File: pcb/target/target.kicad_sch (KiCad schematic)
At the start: 4 parts, among them J1 Pogo_01x06_female, J2 Pogo_01x06_male, U1 ATtiny3216-S

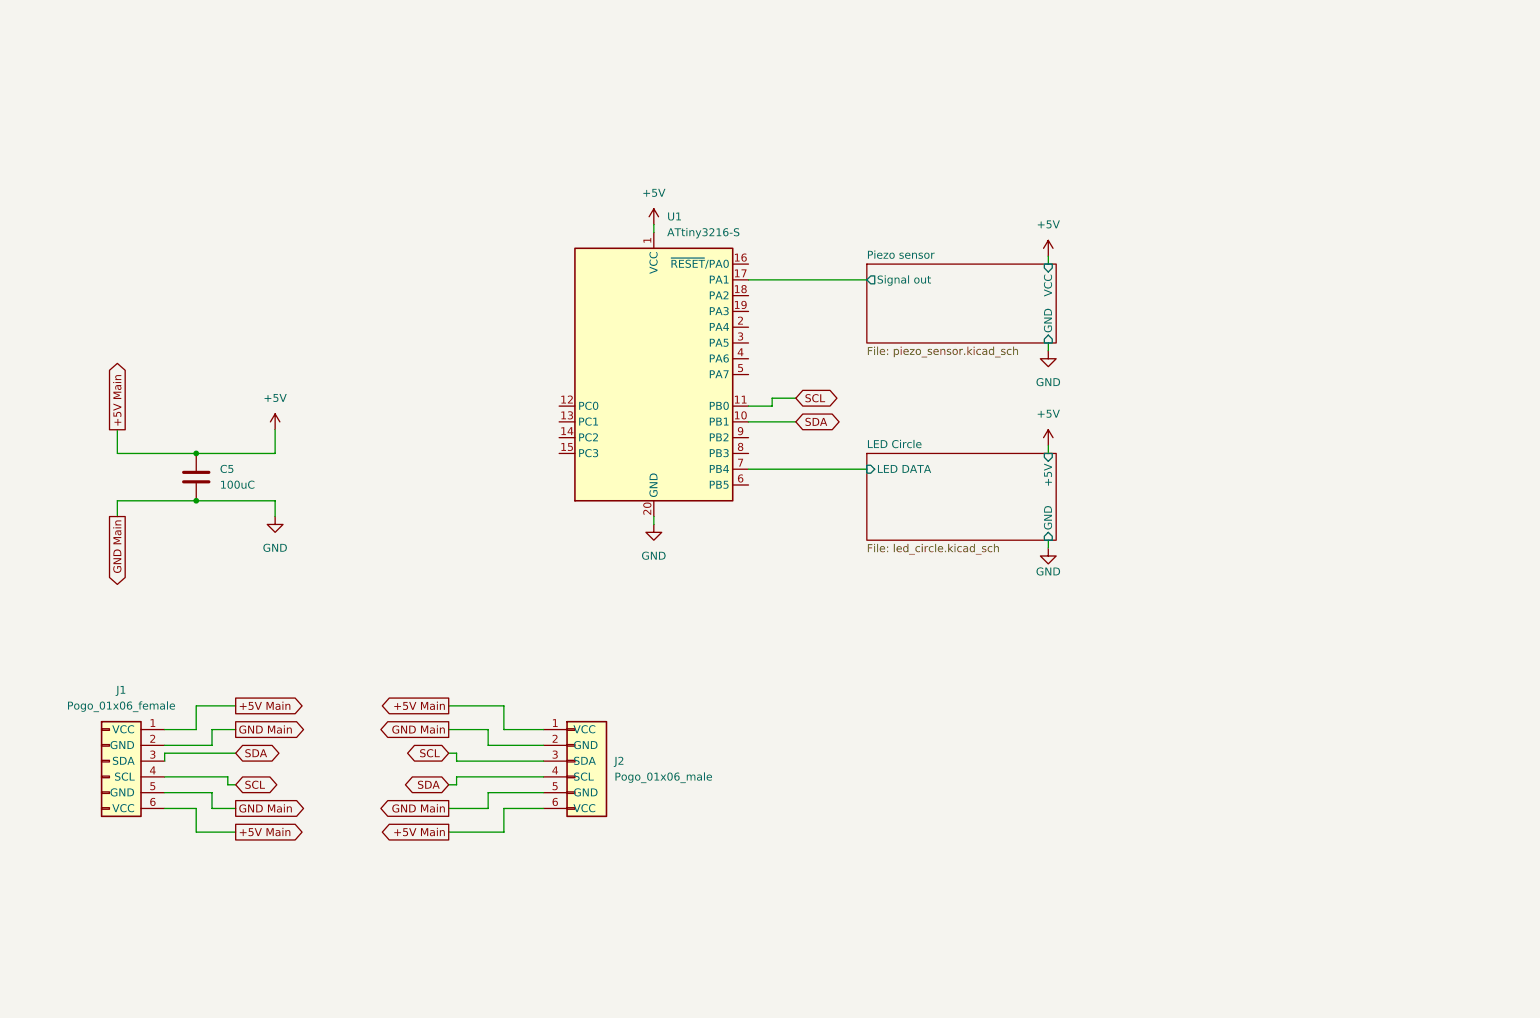
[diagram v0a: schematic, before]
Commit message: added updi connector
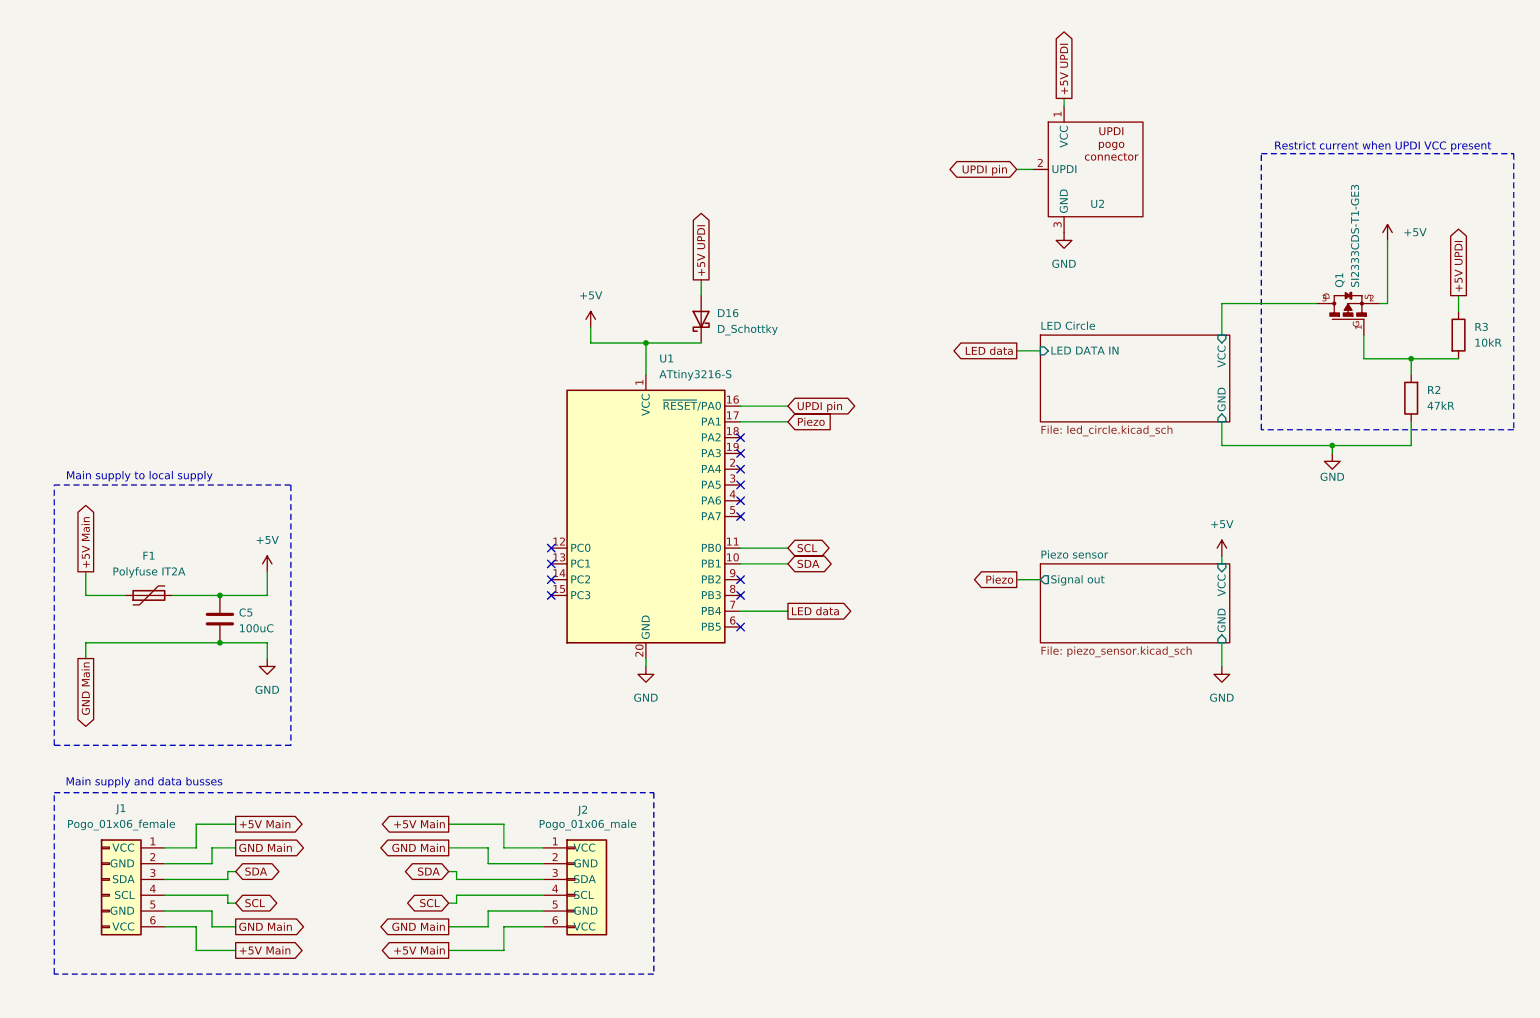
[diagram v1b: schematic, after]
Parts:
- added D16: D_Schottky, custom_footprints:BAT54_SOT23, symbol Device:D_Schottky
- added F1: Polyfuse IT2A, symbol Device:Polyfuse
- added Q1: SI2333CDS-T1-GE3, custom_footprints:SOT23, symbol SI2333CD:SI2333CDS-T1-GE3
- added R2: 47kR, symbol Device:R
- added R3: 10kR, symbol Device:R
- added U2: ~, updi_pogo:P2,54_MH3_pogo_updi, symbol updi_pogo:updi_pogo_connector
- J1, J2: footprint (none) -> Connector_Wire:SolderWire-1sqmm_1x06_P5.4mm_D1.4mm_OD2.7mm
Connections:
- net +5V: now also D16.1 (K), F1.2, Q1.2; no longer J1.1 (VCC), J1.6 (VCC), J2.1 (VCC), J2.6 (VCC)
- net GND: now also R2.1, U2.3 (GND)
- net SCL: now also J2.4 (SCL); no longer J2.3 (SDA)
- net SDA: now also J2.3 (SDA); no longer J2.4 (SCL)
- net UPDI pin: now reaches U1.16 (~{RESET}/PA0)
- net UPDI pin: now also U2.2 (UPDI)
- net LED Circle/LED DATA renamed LED data
- net Piezo sensor/Signal out renamed Piezo
- new net: Q1.1, R2.2, R3.2
- new net +5V Main: F1.1, J1.1 (VCC), J1.6 (VCC), J2.1 (VCC), J2.6 (VCC)
- new net +5V UPDI: D16.2 (A), R3.1, U2.1 (VCC)
- new net LED Circle/VCC: Q1.3
- no-connect marks 0 -> 13
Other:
- sheet LED Circle ports: added LED DATA IN, VCC; removed +5V, LED DATA
- note added: "Main supply and data busses"
- note added: "Main supply to local supply"
- note added: "Restrict current when UPDI VCC present"
- moved on the sheet: C5, J1, J2, U1

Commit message: fixed some footprint issues
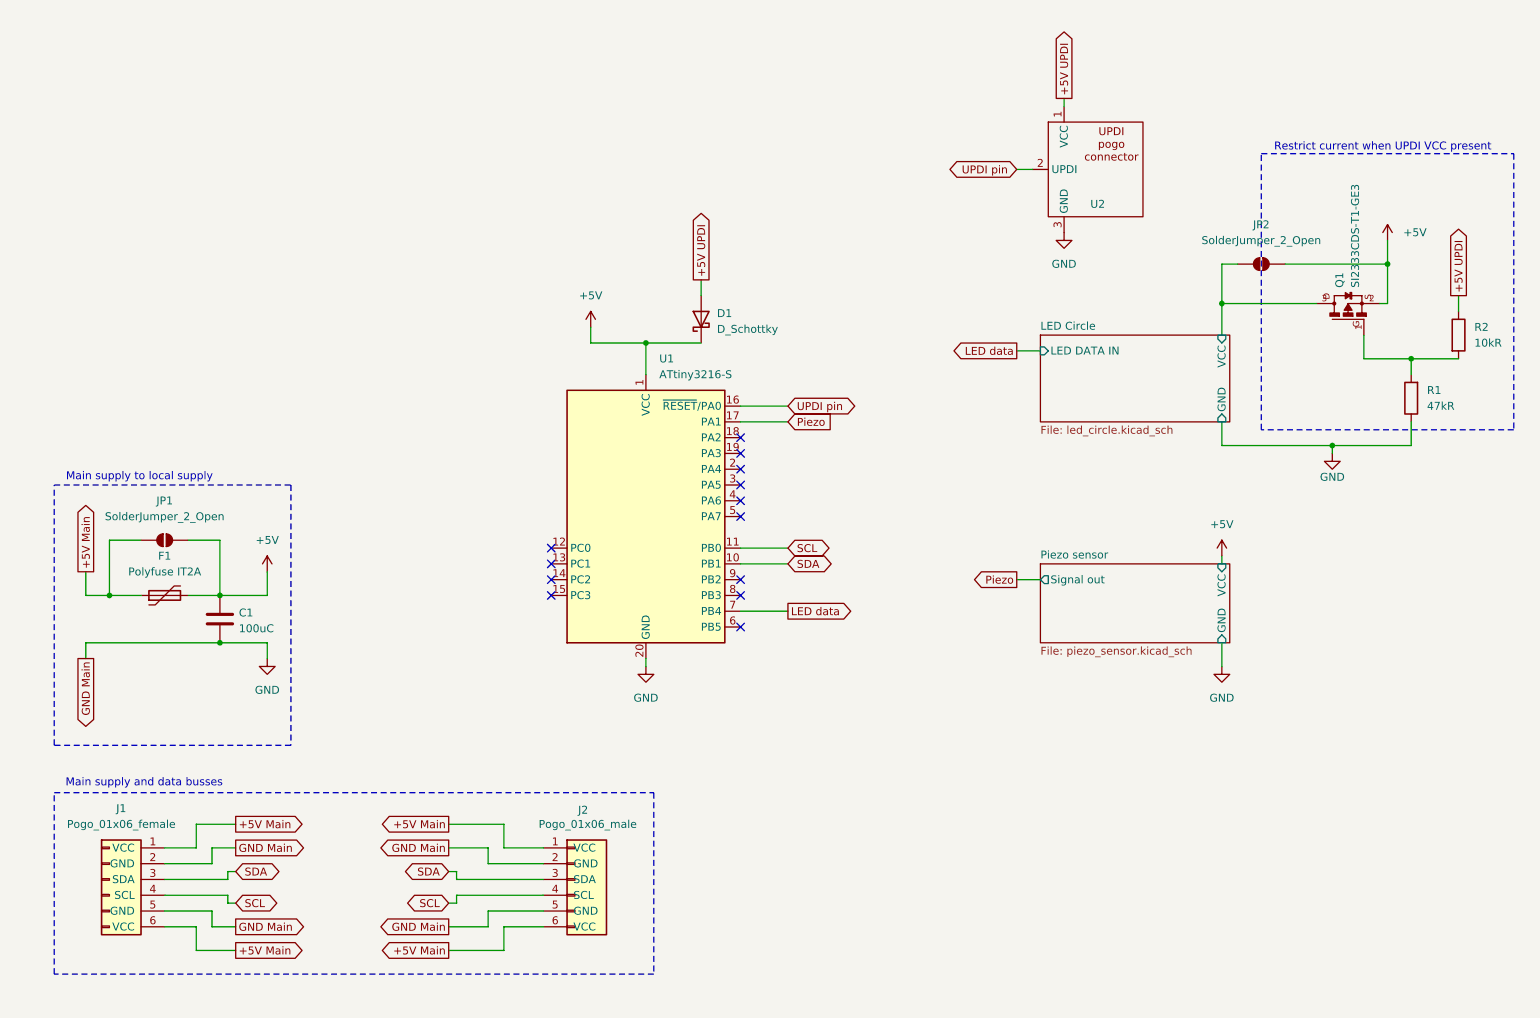
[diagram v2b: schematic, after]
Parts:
- added JP1, JP2: SolderJumper_2_Open, Jumper:SolderJumper-2_P1.3mm_Open_TrianglePad1.0x1.5mm, symbol Jumper:SolderJumper_2_Open
- F1: footprint (none) -> Fuse:Fuse_2920_7451Metric
- R1: renamed from R2; footprint (none) -> Resistor_SMD:R_1206_3216Metric
- R2: renamed from R3; footprint (none) -> Resistor_SMD:R_1206_3216Metric
- renumbered C5 to C1, D16 to D1
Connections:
- net +5V: now also JP1.2 (B), JP2.2 (B)
- net +5V Main: now also JP1.1 (A)
- net LED Circle/VCC: now also JP2.1 (A)
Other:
- moved on the sheet: F1

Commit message: finishing up target pcb
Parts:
- J1, J2: footprint Connector_Wire:SolderWire-1sqmm_1x06_P5.4mm_D1.4mm_OD2.7mm -> custom_footprints:01x06 SMD 4x4mm pad
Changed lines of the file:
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@@
 			)
 		)
-		(property "Footprint" "Connector_Wire:SolderWire-1sqmm_1x06_P5.4mm_D1.4mm_OD2.7mm"
+		(property "Footprint" "custom_footprints:01x06 SMD 4x4mm pad"
 			(at 101.6 175.26 0)
 			(effects
@@
 			)
 		)
-		(property "Footprint" "Connector_Wire:SolderWire-1sqmm_1x06_P5.4mm_D1.4mm_OD2.7mm"
+		(property "Footprint" "custom_footprints:01x06 SMD 4x4mm pad"
 			(at 26.67 175.26 0)
 			(effects

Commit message: retraced target pcb
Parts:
- removed JP1: SolderJumper_2_Open, Jumper:SolderJumper-2_P1.3mm_Open_TrianglePad1.0x1.5mm, symbol Jumper:SolderJumper_2_Open
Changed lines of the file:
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@@
-	)
-	(junction
-		(at 26.67 129.54)
-		(diameter 0)
-		(color 0 0 0 0)
 	)
 	(junction
@@
 	(wire
 		(pts
-			(xy 44.45 120.65) (xy 44.45 129.54)
-		)
-		(stroke
-			(width 0)
-			(type default)
-		)
-	)
-	(wire
-		(pts
 			(xy 220.98 82.55) (xy 205.74 82.55)
 		)
@@
 	(wire
 		(pts
-			(xy 39.37 120.65) (xy 44.45 120.65)
-		)
-		(stroke
-			(width 0)
-			(type default)
-		)
-	)
-	(wire
-		(pts
 			(xy 128.27 121.92) (xy 135.89 121.92)
 		)
@@
 	(wire
 		(pts
-			(xy 26.67 120.65) (xy 26.67 129.54)
-		)
-		(stroke
-			(width 0)
-			(type default)
-		)
-	)
-	(wire
-		(pts
 			(xy 205.74 105.41) (xy 223.52 105.41)
 		)
@@
 	(wire
 		(pts
-			(xy 22.86 129.54) (xy 26.67 129.54)
+			(xy 22.86 129.54) (xy 31.75 129.54)
 		)
 		(stroke
@@
 	(wire
 		(pts
-			(xy 31.75 120.65) (xy 26.67 120.65)
-		)
-		(stroke
-			(width 0)
-			(type default)
-		)
-	)
-	(wire
-		(pts
 			(xy 45.72 175.26) (xy 35.56 175.26)
 		)
@@
 		(pts
 			(xy 205.74 76.2) (xy 205.74 82.55)
-		)
-		(stroke
-			(width 0)
-			(type default)
-		)
-	)
-	(wire
-		(pts
-			(xy 26.67 129.54) (xy 31.75 129.54)
 		)
 		(stroke
@@
 					(unit 1)
 				)
-			)
-		)
-	)
-	(symbol
-		(lib_id "Jumper:SolderJumper_2_Open")
-		(at 35.56 120.65 0)
-		(unit 1)
-		(exclude_from_sim no)
-		(in_bom no)
-		(on_board yes)
-		(dnp no)
-		(fields_autoplaced yes)
-		(property "Reference" "JP1"
-			(at 35.56 114.3 0)
-			(effects
-				(font
-					(size 1.27 1.27)
-				)
-			)
-		)
-		(property "Value" "SolderJumper_2_Open"
-			(at 35.56 116.84 0)
-			(effects
-				(font
-					(size 1.27 1.27)
-				)
-			)
-		)
-		(property "Footprint" "Jumper:SolderJumper-2_P1.3mm_Open_TrianglePad1.0x1.5mm"
-			(at 35.56 120.65 0)
-			(effects
-				(font
-					(size 1.27 1.27)
-				)
-				(hide yes)
-			)
-		)
-		(property "Datasheet" "~"
-			(at 35.56 120.65 0)
-			(effects
-				(font
-					(size 1.27 1.27)
-				)
-				(hide yes)
-			)
-		)
-		(property "Description" "Solder Jumper, 2-pole, open"
-			(at 35.56 120.65 0)
-			(effects
-				(font
-					(size 1.27 1.27)
-				)
-				(hide yes)
-			)
-		)
-		(pin "2"
-		)
-		(pin "1"
-		)
-		(instances
-			(project ""
-				(path "/1c02f793-f381-44cb-838a-dbb787484d0c"
-					(reference "JP1")
-					(unit 1)
-				)

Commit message: added lcsc numbers to all components and added ESD protection
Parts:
- removed U1: ATtiny3216-S, Package_SO:SOIC-20W_7.5x12.8mm_P1.27mm, symbol MCU_Microchip_ATtiny:ATtiny3216-S
- added U1: ~, custom_footprints:WQFN-24_L4.0-W4.0-P0.50-TL-EP2.6, symbol custom_symbols:ATTINY3217-MFR
- C1: value 100uC -> 100u; LCSC (none) -> C15008
- D1: value D_Schottky -> SS54; footprint custom_footprints:BAT54_SOT23 -> Diode_SMD:D_SMA; LCSC (none) -> C20609300
- F1: LCSC (none) -> C22366130
- Q1: value SI2333CDS-T1-GE3 -> SI2333CDS-HXY; LCSC (none) -> C18198389
- R1: footprint Resistor_SMD:R_1206_3216Metric -> Resistor_SMD:R_0805_2012Metric; LCSC (none) -> C2907330
- R2: footprint Resistor_SMD:R_1206_3216Metric -> Resistor_SMD:R_0805_2012Metric; LCSC (none) -> C84376
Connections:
- net +5V: now also U1.4 (VDD)
- net +5V Main: no longer J2.1 (VCC), J2.6 (VCC)
- net GND: now also U1.25 (GND), U1.3 (GND)
- net LED data: now also U1.24 (PA1)
- net Piezo: now also U1.8 (PA7)
- net SCL: now also U1.16 (PB0); no longer J2.4 (SCL)
- net SDA: now also U1.15 (PB1); no longer J2.3 (SDA)
- net UPDI pin: now also U1.23 (PA0/RESET#/UPDI)
- new net ESD/5V OUT: J2.1 (VCC)
- new net ESD/5V OUT 2: J2.6 (VCC)
- new net ESD/SCL OUT: J2.4 (SCL)
- new net ESD/SDA OUT: J2.3 (SDA)
- no-connect marks 13 -> 0
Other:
- added sheet ESD (esd.kicad_sch)
- note added: "*Might be exposed, when it is the last Target in Series*"
- moved on the sheet: C1, D1, F1, J1, J2

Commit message: finished all pcbs by adjusting traces acording to 1oz copper weight
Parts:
- J1, J2, U2: now left out of the parts list
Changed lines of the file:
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@@
 		(unit 1)
 		(exclude_from_sim no)
-		(in_bom yes)
+		(in_bom no)
 		(on_board yes)
 		(dnp no)
@@
 		(unit 1)
 		(exclude_from_sim no)
-		(in_bom yes)
+		(in_bom no)
 		(on_board yes)
 		(dnp no)
@@
 		(unit 1)
 		(exclude_from_sim no)
-		(in_bom yes)
+		(in_bom no)
 		(on_board yes)
 		(dnp no)
